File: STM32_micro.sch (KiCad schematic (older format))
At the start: 47 parts, among them J3 Conn_02x06_Odd_Even, J4 Conn_02x10_Odd_Even, U4 FSM1LPTR, U5 STM32F722ZET, U6 LSM9DS1, Y1 ABM8G-16.000MHZ-B4Y-T, Y2 Crystal

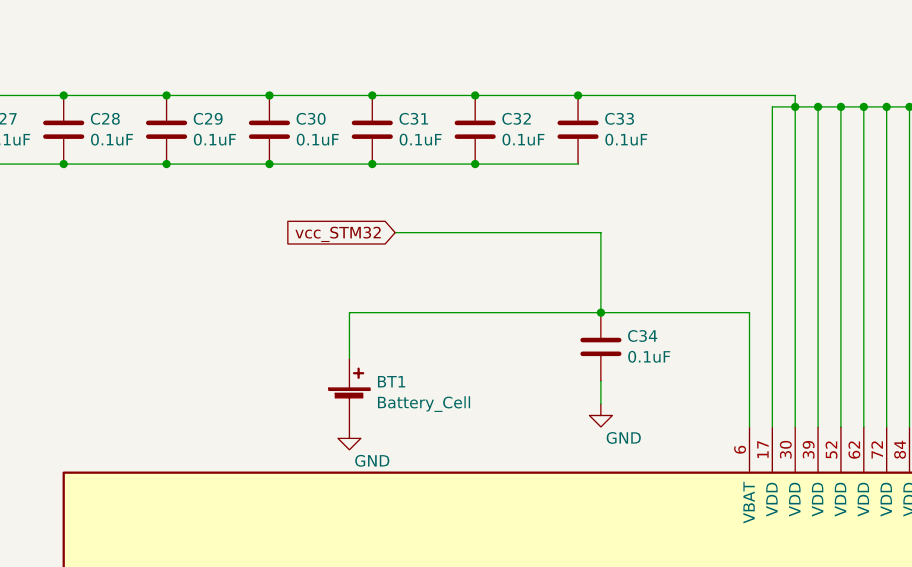
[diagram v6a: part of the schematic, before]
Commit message: diseño de esquematico arreglo de flechas rojas
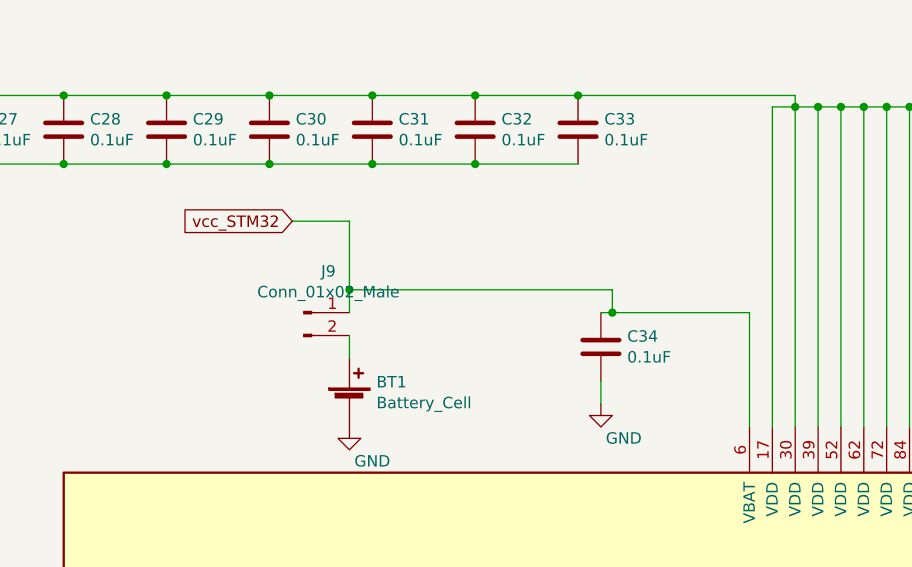
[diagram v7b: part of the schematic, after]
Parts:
- added J9: Conn_01x02_Male, Connector_PinHeader_2.54mm:PinHeader_1x02_P2.54mm_Vertical, symbol Connector_01x18:Conn_01x02_Male
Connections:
- wire segments 370 -> 373
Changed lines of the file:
@@
 Wire Wire Line
 	10750 2800 10750 1400
-Text GLabel 9100 1950 0    50   Input ~ 0
+Text GLabel 8650 1900 0    50   Input ~ 0
 vcc_STM32
 $Comp
@@
 $EndComp
 Wire Wire Line
-	10000 1950 10000 2300
-Wire Wire Line
 	10650 2800 10650 2300
 Wire Wire Line
-	10650 2300 10000 2300
-Wire Wire Line
-	8900 2300 8900 2500
+	10650 2300 10050 2300
 $Comp
 L power:GND #PWR033
@@
 Wire Wire Line
 	18350 8050 17650 8050
-Connection ~ 10000 2300
 Wire Wire Line
 	6100 4700 6350 4700
@@
 Wire Wire Line
 	6350 5350 7250 5350
-Wire Wire Line
-	9100 1950 10000 1950
-Wire Wire Line
-	8900 2300 10000 2300
 Text GLabel 19350 12950 3    50   Input ~ 0
 VCC_5V
@@
 Wire Wire Line
 	16350 7100 17000 7100
+Wire Wire Line
+	8650 1900 8900 1900
+Wire Wire Line
+	8900 2200 10050 2200
+Wire Wire Line
+	10050 2200 10050 2300
+Connection ~ 10050 2300
+Wire Wire Line
+	10050 2300 10000 2300
+Wire Wire Line
+	8900 1900 8900 2200
+$Comp
+L Connector_01x18:Conn_01x02_Male J9
+U 1 1 5D073F54
+P 8700 2300
+F 0 "J9" H 8808 2481 50  0000 C CNN
+F 1 "Conn_01x02_Male" H 8808 2390 50  0000 C CNN
+F 2 "Connector_PinHeader_2.54mm:PinHeader_1x02_P2.54mm_Vertical" H 8700 2300 50  0001 C CNN
+F 3 "~" H 8700 2300 50  0001 C CNN
+	1    8700 2300
+	1    0    0    -1
+$EndComp
+Wire Wire Line
+	8900 2300 8900 2200
+Connection ~ 8900 2200
+Wire Wire Line
+	8900 2500 8900 2400
 $EndSCHEMATC

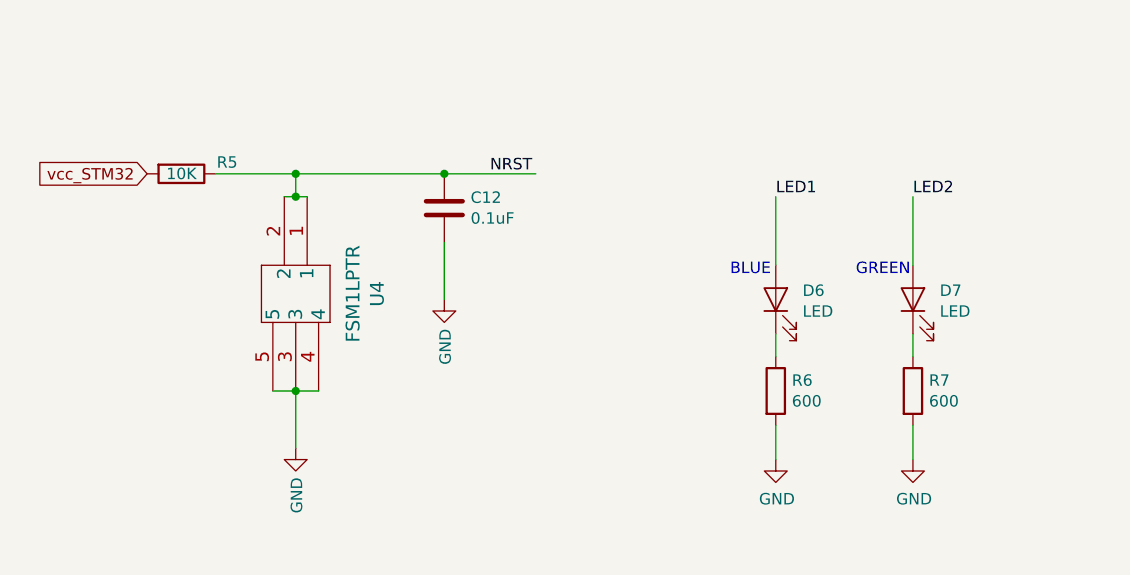
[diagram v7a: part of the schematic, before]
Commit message: programacion luego del diseño del embebido
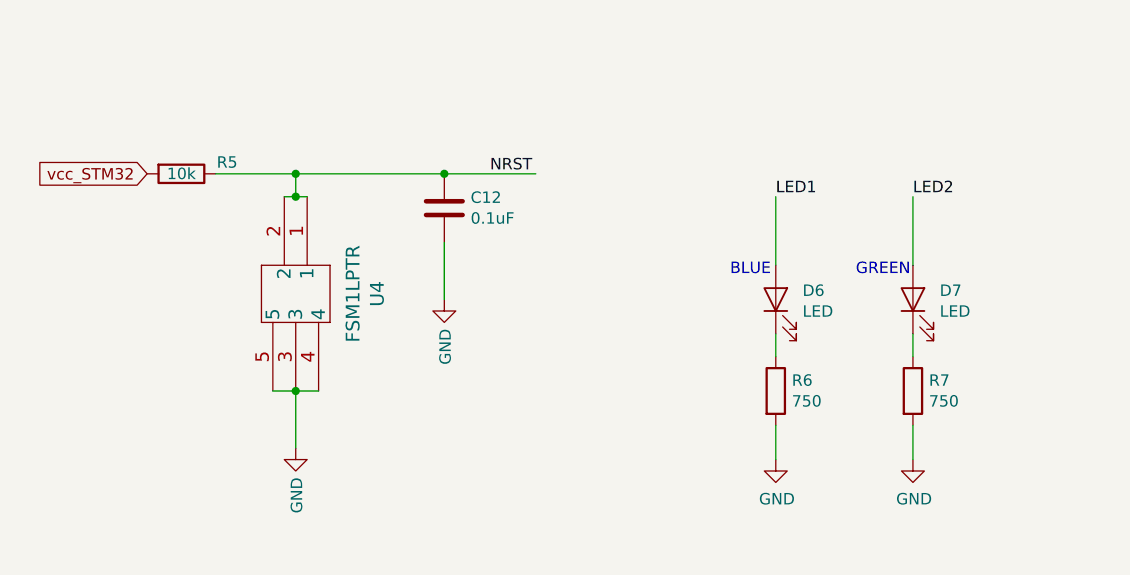
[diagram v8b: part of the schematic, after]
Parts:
- R5: value 10K -> 10k
- R6, R7: value 600 -> 750
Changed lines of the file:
@@
 P 2100 6500
 F 0 "R5" V 2050 6700 50  0000 C CNN
-F 1 "10K" V 2100 6500 50  0000 C CNN
+F 1 "10k" V 2100 6500 50  0000 C CNN
 F 2 "Resistor_SMD:R_0603_1608Metric_Pad1.05x0.95mm_HandSolder" V 2030 6500 50  0001 C CNN
 F 3 "~" H 2100 6500 50  0001 C CNN
@@
 AR Path="/5CD05F2F/5EEFFBC1" Ref="R6"  Part="1"
 F 0 "R6" H 4770 7496 50  0000 L CNN
-F 1 "600" H 4770 7405 50  0000 L CNN
+F 1 "750" H 4770 7405 50  0000 L CNN
 F 2 "Resistor_SMD:R_0603_1608Metric_Pad1.05x0.95mm_HandSolder" V 4630 7450 50  0001 C CNN
 F 3 "~" H 4700 7450 50  0001 C CNN
-F 4 "" H 4700 7450 50  0001 C CNN "Digikey"
 	1    4700 7450
 	1    0    0    -1
@@
 AR Path="/5CD05F2F/5EF32406" Ref="R7"  Part="1"
 F 0 "R7" H 5370 7496 50  0000 L CNN
-F 1 "600" H 5370 7405 50  0000 L CNN
+F 1 "750" H 5370 7405 50  0000 L CNN
 F 2 "Resistor_SMD:R_0603_1608Metric_Pad1.05x0.95mm_HandSolder" V 5230 7450 50  0001 C CNN
 F 3 "~" H 5300 7450 50  0001 C CNN
-F 4 "" H 5300 7450 50  0001 C CNN "Digikey"
 	1    5300 7450
 	1    0    0    -1
